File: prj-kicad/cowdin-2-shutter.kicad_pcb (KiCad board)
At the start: 2 copper layers, 33 x 86.5 mm, 6 parts, among them P2 CONN_3, P4 CONN_3

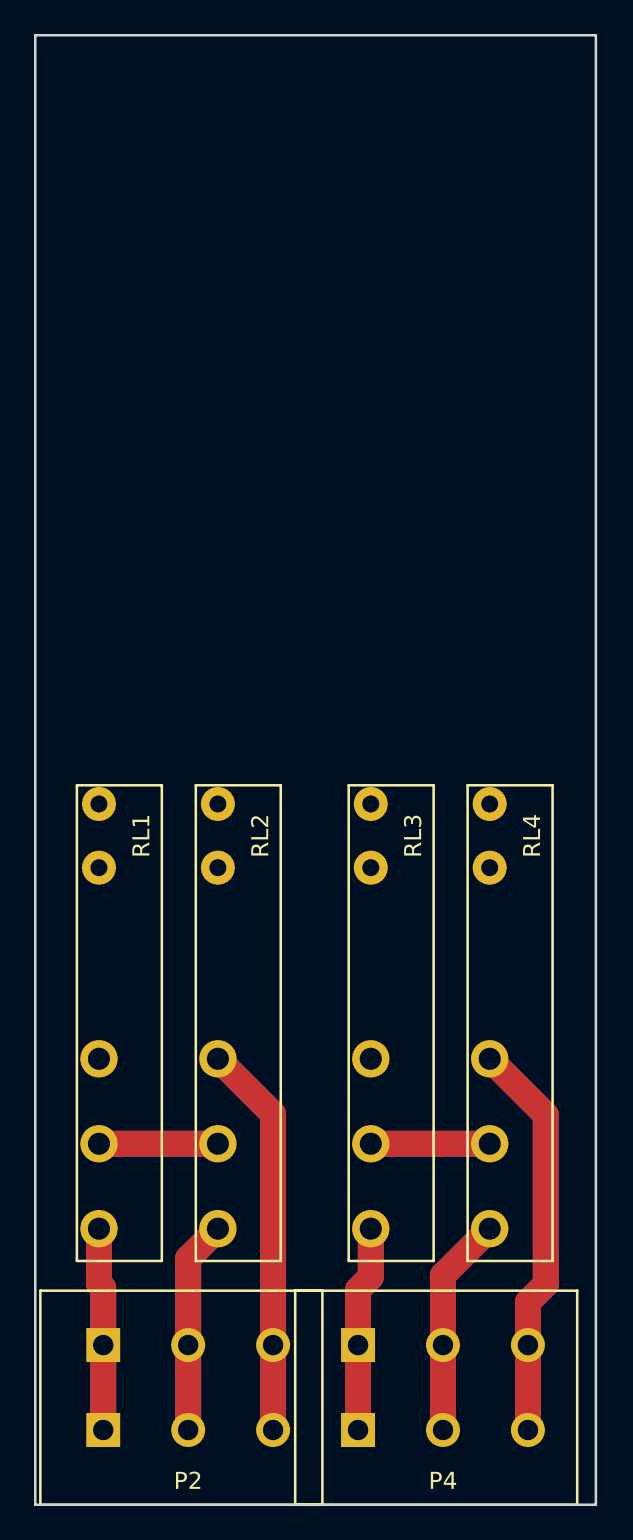
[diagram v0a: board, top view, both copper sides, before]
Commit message: = ADD: Insert power supply for wide VIN (5-40V) to 5V internal
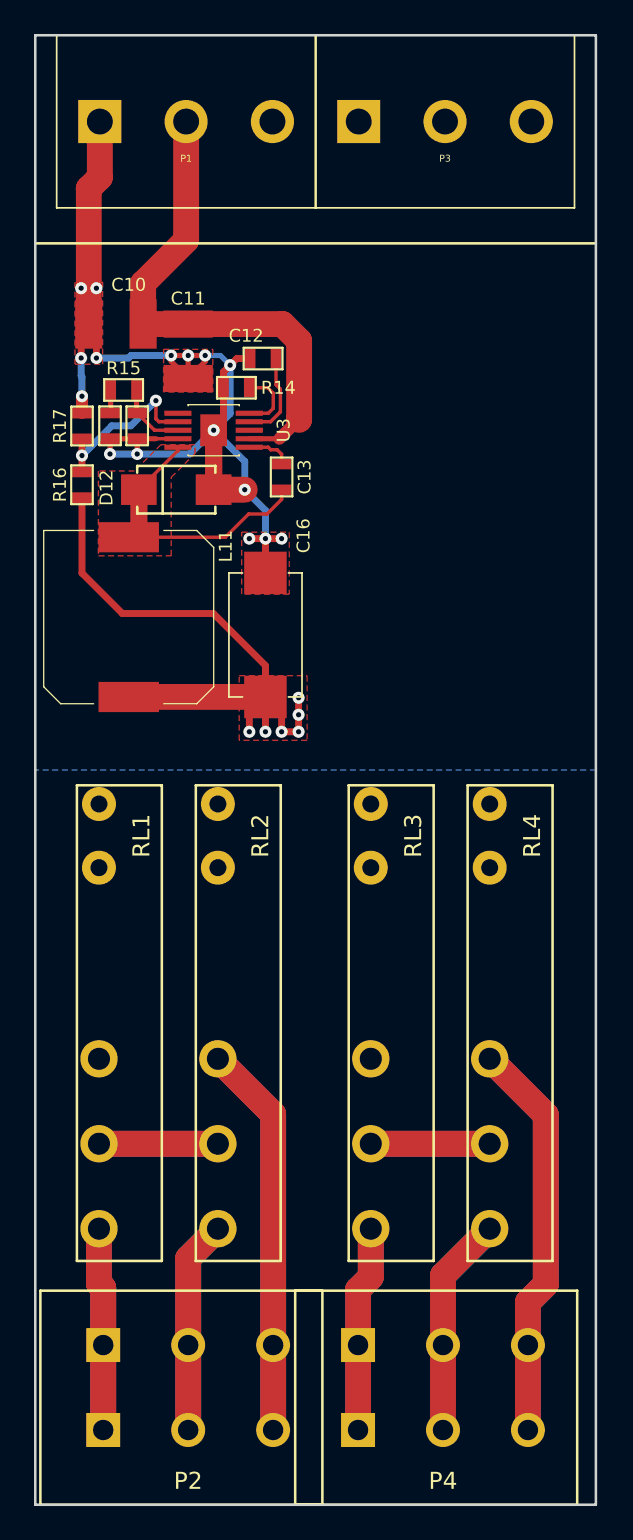
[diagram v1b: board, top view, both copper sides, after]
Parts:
- added C10: 10uF, cowdin-2-shutter:SMD1210, F.Cu at (136.8, 78.8)
- added C11: C, cowdin-2-shutter:SMD1210, F.Cu at (141.0, 80.3)
- added C12: 10nF, cowdin-2-shutter:SMD0603, F.Cu at (145.4, 80.8)
- added C13: 100nF, cowdin-2-shutter:SMD0603, F.Cu at (146.5, 87.8)
- added C14: n/a, cowdin-2-shutter:SMD0603, F.Cu at (138.0, 84.7)
- added C15: 4,7nF, cowdin-2-shutter:SMD0603, F.Cu at (136.4, 84.7)
- added C16: 220uF, cowdin-2-shutter:C_TPB_D4, F.Cu at (145.6, 97.0)
- added D12: MBRA340, cowdin-2-shutter:DO214AC, F.Cu at (140.3, 88.5)
- added L11: 27uH, cowdin-2-shutter:I_MSS1048, F.Cu at (137.5, 96.0)
- added P1: CONN_3, cowdin-2-shutter:CONN_MC000035, F.Cu at (140.9, 66.8)
- added P3: CONN_3, cowdin-2-shutter:CONN_MC000035, F.Cu at (156.1, 66.8)
- added R14: 100k, cowdin-2-shutter:SMD0603, F.Cu at (143.8, 82.5)
- added R15: 20k, cowdin-2-shutter:SMD0603, F.Cu at (137.2, 82.6)
- added R16: 52,3k, cowdin-2-shutter:SMD0603, F.Cu at (134.8, 88.2)
- added R17: 10k, cowdin-2-shutter:SMD0603, F.Cu at (134.8, 84.8)
- added U3: TPS54060A, cowdin-2-shutter:MSOP10p, F.Cu at (142.5, 85.0)
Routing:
- net GND: track 0.00 -> 77.5 mm, vias 0 -> 16
- net 5V: track 0.00 -> 36.0 mm, vias 0 -> 6
- net VIn: track 0.00 -> 30.6 mm
- net /V5_SW: track 0.00 -> 17.0 mm
- net Net-(R16-Pad2): track 0.00 -> 10.1 mm, vias 0 -> 2
- net Net-(C12-Pad1): track 0.00 -> 5.32 mm
- net Net-(C14-Pad1): track 0.00 -> 4.19 mm
- net Net-(R14-Pad1): track 0.00 -> 3.96 mm
- net Net-(C13-Pad1): track 0.00 -> 2.65 mm
- net Net-(C15-Pad1): track 0.00 -> 1.36 mm
- added copper zone on F.Cu, net 5V
- added copper zone on B.Cu, net GND
- added copper zone on F.Cu, net GND
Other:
- copper layers 2 -> 4
- net class Default: via_dia 0.8 -> 0.6
- rule pad_to_mask_clearance: 0.051 -> 0.2
- rule trace_min: 0.2 -> 0.1524

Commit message: = ADD: Insert processor and CAN interface (sch & routing)
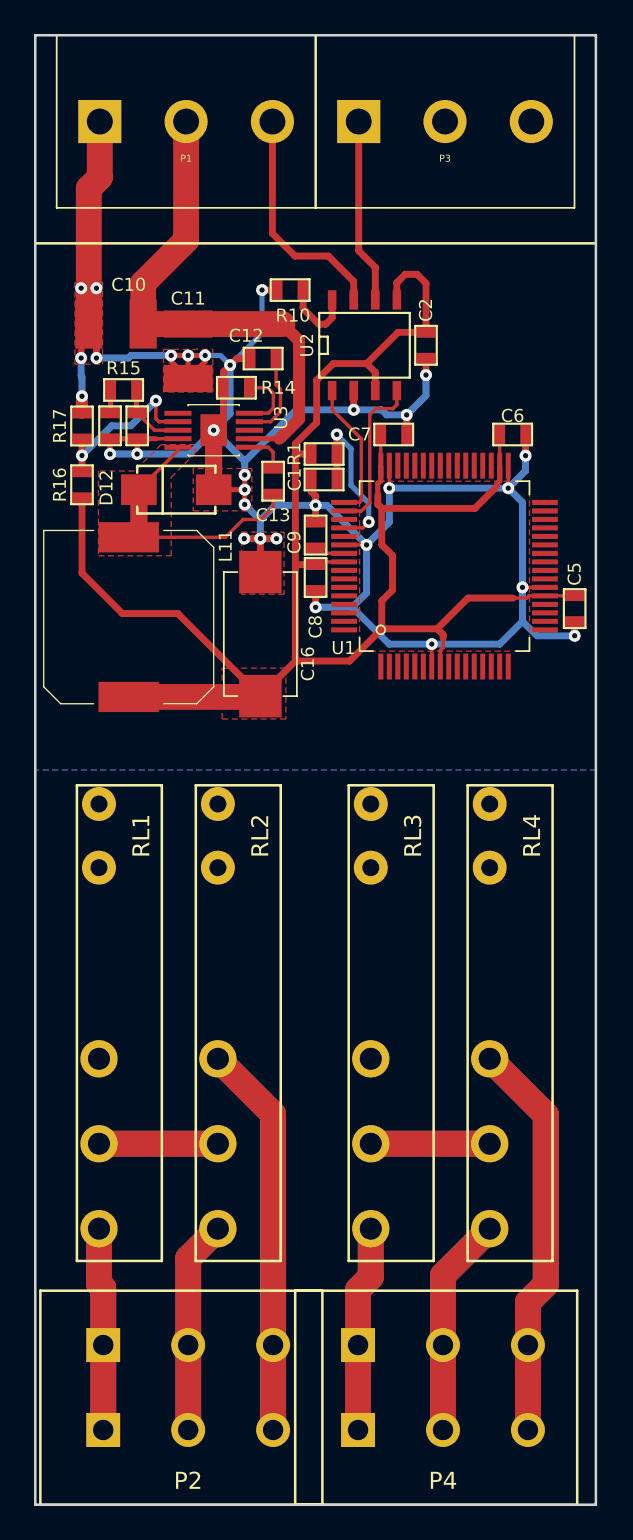
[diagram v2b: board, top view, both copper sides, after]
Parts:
- added C1: 1uF, cowdin-2-shutter:SMD0603, F.Cu at (149.0, 87.9)
- added C2: 100nF, cowdin-2-shutter:SMD0603, F.Cu at (155.0, 80.0)
- added C5: 100nF, cowdin-2-shutter:SMD0603, F.Cu at (163.8, 95.5)
- added C6: 100nF, cowdin-2-shutter:SMD0603, F.Cu at (160.1, 85.2)
- added C7: 100nF, cowdin-2-shutter:SMD0603, F.Cu at (153.1, 85.2)
- added C8: 100nF, cowdin-2-shutter:SMD0603, F.Cu at (148.5, 93.7)
- added C9: 100nF, cowdin-2-shutter:SMD0603, F.Cu at (148.5, 91.2)
- added R1: 10k, cowdin-2-shutter:SMD0603, F.Cu at (149.0, 86.4)
- added R10: 10k, cowdin-2-shutter:SMD0603, F.Cu at (147.0, 76.8)
- added U1: ATSAMC21J, cowdin-2-shutter:TQFP64, F.Cu at (156.1, 93.0)
- added U2: MCP2562, cowdin-2-shutter:SOIC-8E, F.Cu at (151.4, 80.0)
- moved C13 0.56 mm to (146.0, 88.0)
- moved C16 0.30 mm to (145.2, 97.0)
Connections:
- P1 pad 3: Net-(P1-Pad3) -> CAN_H
- P3 pad 1: Net-(P3-Pad1) -> CAN_L
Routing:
- net GND: track 77.5 -> 162.9 mm, vias 16 -> 31
- net 5V: track 36.0 -> 108.3 mm, vias 6 -> 0
- net CAN_H: track 0.00 -> 13.6 mm
- net CAN_L: track 0.00 -> 10.9 mm
- net RESET: track 0.00 -> 10.2 mm, vias 0 -> 2
- net CAN0_RX: track 0.00 -> 9.55 mm
- net CAN0_TX: track 0.00 -> 8.24 mm
- net Net-(R10-Pad1): track 0.00 -> 4.39 mm
- net Net-(C9-Pad2): track 0.00 -> 1.81 mm

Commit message: = ADD: Insert input and output interfaces
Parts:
- added C3: 100nF, cowdin-2-shutter:SMD0603, F.Cu at (157.8, 83.0)
- added C4: 100nF, cowdin-2-shutter:SMD0603, F.Cu at (162.8, 87.8)
- added D1: D, cowdin-2-shutter:SOD-123, F.Cu at (137.0, 103.8)
- added D2: D, cowdin-2-shutter:SOD-123, F.Cu at (144.0, 103.8)
- added D3: D, cowdin-2-shutter:SOD-123, F.Cu at (153.0, 104.0)
- added D4: D, cowdin-2-shutter:SOD-123, F.Cu at (160.0, 104.0)
- added D5: D_Schottky, cowdin-2-shutter:SOD-123, F.Cu at (158.5, 78.2)
- added D6: SMAJ5.0, cowdin-2-shutter:DO214AC, F.Cu at (155.8, 78.8)
- added D7: D_Schottky, cowdin-2-shutter:SOD-123, F.Cu at (162.8, 84.5)
- added D8: SMAJ5.0, cowdin-2-shutter:DO214AC, F.Cu at (162.1, 78.8)
- added Q1: Q_NMOS, cowdin-2-shutter:SOT23-3, F.Cu at (148.5, 113.2)
- added Q2: Q_NMOS, cowdin-2-shutter:SOT23-3, F.Cu at (148.5, 108.0)
- added Q3: Q_NMOS, cowdin-2-shutter:SOT23-3, F.Cu at (148.5, 104.0)
- added Q4: Q_NMOS, cowdin-2-shutter:SOT23-3, F.Cu at (162.8, 101.0)
- added TP1: CONN_1, cowdin-2-shutter:TP_SMD, B.Cu at (153.8, 93.9)
- added TP2: CONN_1, cowdin-2-shutter:TP_SMD, B.Cu at (153.8, 96.4)
- added TP3: CONN_1, cowdin-2-shutter:TP_SMD, B.Cu at (153.8, 91.4)
- added TP4: CONN_1, cowdin-2-shutter:TP_SMD, B.Cu at (153.8, 88.8)
- P2, P4: footprint cowdin-2-shutter:CONN_691411710003 -> cowdin-2-shutter:CONN_MC000035
- moved C2 3.34 mm to (155.0, 83.3)
- moved P2 1.82 mm to (140.9, 143.2)
- moved P4 1.82 mm to (156.1, 143.2)
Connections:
- P3 pad 2: Net-(P3-Pad2) -> IN_1
- P3 pad 3: Net-(P3-Pad3) -> IN_2
- RL1 pad A2: Net-(RL1-PadA2) -> VIn
- RL2 pad A1: Net-(RL2-PadA1) -> VIn
- RL3 pad A2: Net-(RL3-PadA2) -> VIn
- RL4 pad A1: Net-(RL4-PadA1) -> VIn
- U1 pad 16: Net-(U1-Pad16) -> REL4
- U1 pad 2: Net-(U1-Pad2) -> REL3
- U1 pad 3: Net-(U1-Pad3) -> REL2
- U1 pad 32: Net-(U1-Pad32) -> IN_UP
- U1 pad 36: Net-(U1-Pad36) -> IN_DN
- U1 pad 4: Net-(U1-Pad4) -> REL1
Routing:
- net VIn: track 30.6 -> 172.3 mm
- net GND: track 162.9 -> 206.6 mm, vias 31 -> 42
- net Net-(D1-Pad1): track 0.00 -> 26.8 mm, vias 0 -> 2
- net IN_2: track 0.00 -> 20.0 mm
- net REL1: track 0.00 -> 17.4 mm, vias 0 -> 2
- net Net-(D2-Pad1): track 0.00 -> 13.3 mm
- net IN_1: track 0.00 -> 12.7 mm
- net Net-(D3-Pad1): track 0.00 -> 12.0 mm
- net REL2: track 0.00 -> 9.71 mm, vias 0 -> 2
- net Net-(D4-Pad1): track 0.00 -> 7.49 mm
- net IN_DN: track 0.00 -> 7.28 mm
- net REL3: track 0.00 -> 6.04 mm
- net SWD_DAT: track 0.00 -> 5.09 mm, vias 0 -> 1
- net IN_UP: track 0.00 -> 4.80 mm
- net SWD_CLK: track 0.00 -> 4.26 mm, vias 0 -> 1
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
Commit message: = ADD: Create production files
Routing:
- added copper zone on F.Cu, net /V5_SW
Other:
- copper layers 4 -> 2
- rule pad_to_mask_clearance: 0.2 -> 0.05
- rule solder_mask_min_width: 0.25 -> 0.05
- board text added: "Agilack CC-by-SA"
- board text added: "cowdin-2-shutter rev1"
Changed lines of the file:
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@@
   (general
     (thickness 1.6)
-    (drawings 17)
+    (drawings 19)
     (tracks 501)
     (zones 0)
@@
   (layers
     (0 F.Cu signal)
-    (1 In1.Cu signal)
-    (2 In2.Cu signal)
     (31 B.Cu signal)
     (32 B.Adhes user)
@@
     (pad_size 0.635 1.143)
     (pad_drill 0)
-    (pad_to_mask_clearance 0.2)
-    (solder_mask_min_width 0.25)
+    (pad_to_mask_clearance 0.05)
+    (solder_mask_min_width 0.05)
+    (pad_to_paste_clearance -0.05)
     (aux_axis_origin 0 0)
     (visible_elements FFFFFFFF)
@@
       (drillshape 0)
       (scaleselection 1)
-      (outputdirectory "../prod/pick_place/"))
+      (outputdirectory "../prod/"))
   )
   (net 0 "")
@@
   (module cowdin-2-shutter:RL_3451 (layer F.Cu)
     (at 135.75 107 270)
-    (fp_text reference RL1 (at 11 2.5 270) (layer F.SilkS)
+    (fp_text reference RL1 (at 1.75 2.5 270) (layer F.SilkS)
       (effects (font (size 1 1) (thickness 0.15)))
     )
@@
   (module cowdin-2-shutter:RL_3451 (layer F.Cu)
     (at 142.75 107 270)
-    (fp_text reference RL2 (at 11 2.25 270) (layer F.SilkS)
+    (fp_text reference RL2 (at 1.75 2.25 270) (layer F.SilkS)
       (effects (font (size 1 1) (thickness 0.15)))
     )
@@
       (rotate (xyz 0 0 0))
     )
+  )
+  (gr_text "Agilack CC-by-SA" (at 163.96 128.18 90) (layer F.Cu)
+    (effects (font (size 1 1) (thickness 0.1524)))
+  )
+  (gr_text "cowdin-2-shutter rev1" (at 133.1 125.81 90) (layer F.Cu)
+    (effects (font (size 1 1) (thickness 0.1524)))
   )
   (dimension 12 (width 0.3) (layer Cmts.User)
@@
   (segment (start 162.75 86.73) (end 163.512 87.492) (width 0.3048) (layer F.Cu) (net 85) (status 800000))
   (segment (start 163.512 87.492) (end 163.512 87.75) (width 0.3048) (layer F.Cu) (net 85) (status C00000))
-  (zone (net 11) (net_name GND) (layer F.Cu) (hatch edge 0.508)
+  (zone (net 20) (net_name /V5_SW) (layer F.Cu) (hatch edge 0.508)
     (connect_pads yes (clearance 0.1524))
     (min_thickness 0.254)
